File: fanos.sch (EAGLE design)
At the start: 20 parts, among them U1 BP2832K

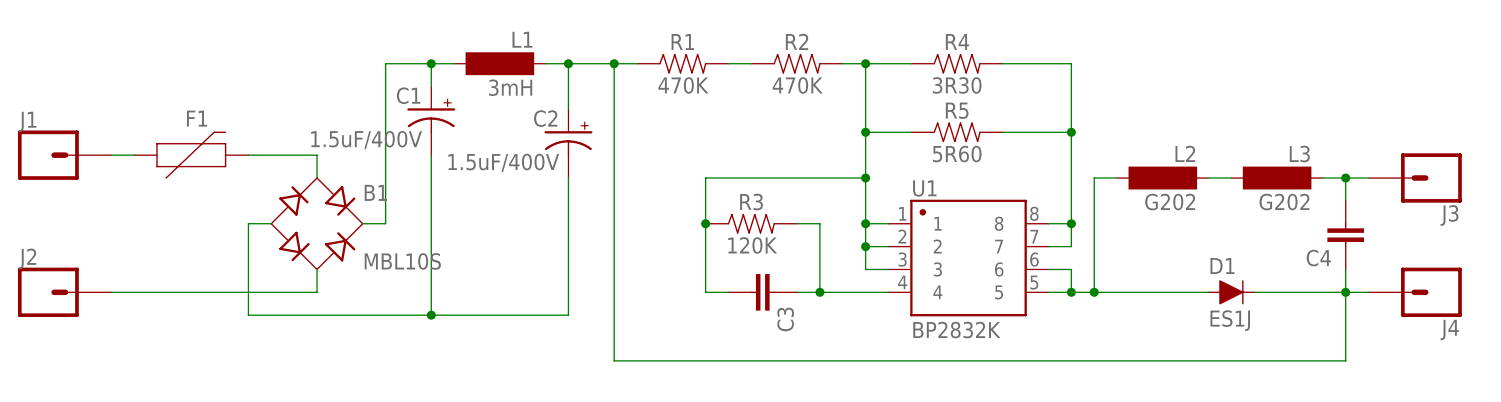
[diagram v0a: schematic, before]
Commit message: Fixed some wiring and added board layout
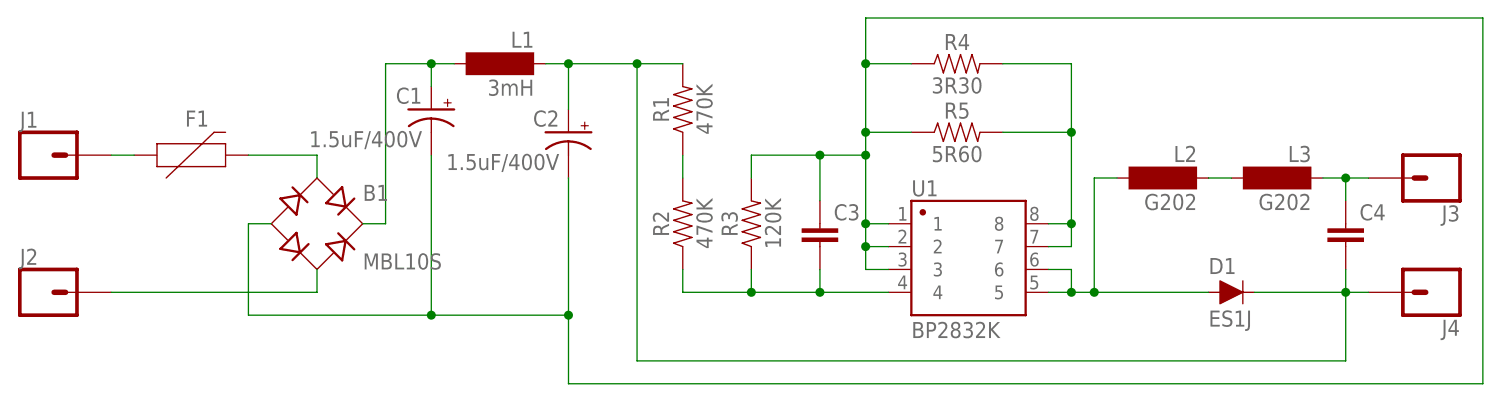
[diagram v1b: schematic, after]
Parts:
- C4: value 22UF-1210-16V-20% -> 0.33UF/330NF-0805-50V-10%; device SparkFun-Capacitors:22UF-1210-16V-20% -> SparkFun-Capacitors:0.33UF/330NF-0805-50V-10%
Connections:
- removed net N$5: C2.+, C4.1, D1.C, J4.1, L1.1, R1.1
- removed net N$7: C3.2, R2.2, R3.1, R4.1, R5.1, U1.1, U1.2, U1.3
- new net N$12: C2.+, C4.2, D1.C, J4.1, L1.1, R1.2
- net N$14: now also C4.1; no longer C4.2
- net N$4: now also C3.1, R3.2, R4.1, R5.1, U1.1, U1.2, U1.3
- net N$8: now also C3.2, R3.1, U1.4; no longer R1.2
- net N$9: now also R1.1, R2.2; no longer C3.1, R3.2, U1.4
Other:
- moved on the sheet: C3, C4, R1, R2, R3
